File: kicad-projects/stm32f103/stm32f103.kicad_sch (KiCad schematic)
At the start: 68 parts, among them J1 Conn_01x20_Male, J2 USB_C_Receptacle, J3 Jack-DC, J4 Conn_02x02_Odd_Even, J5 Conn_01x10_Female, J6 Conn_01x06_Female, J7 Conn_01x08_Female, J8 Conn_01x08_Female, SW1 SW_Push, U1 TPS62175DQC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

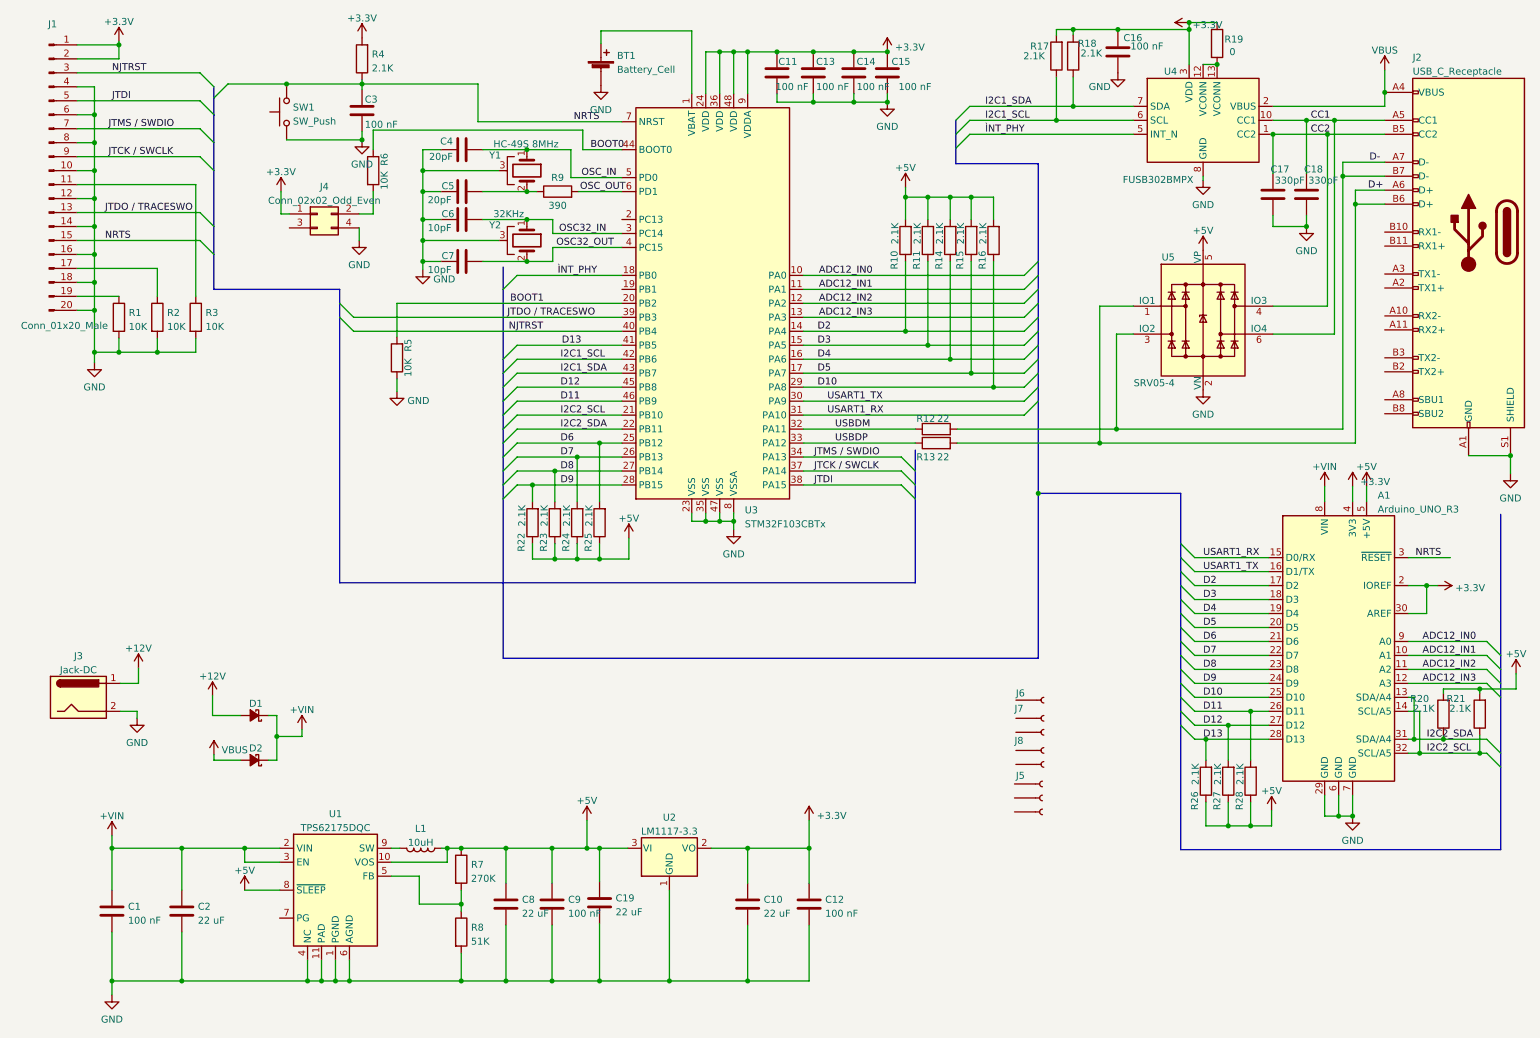
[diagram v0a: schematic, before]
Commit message: pcb: revision bump
stm32f103: revison 2
  - added: D+ to +5V (fixed error: unable to enumerate device)
  - added: usb phy int pin pull up to +3.3v (fixed no irq from phy)
  - moved: JTAG connector is moved to bottom layer

clock-top (nixie shild): revision 1, initial version

removed pf-info-cache (temp kicad file)
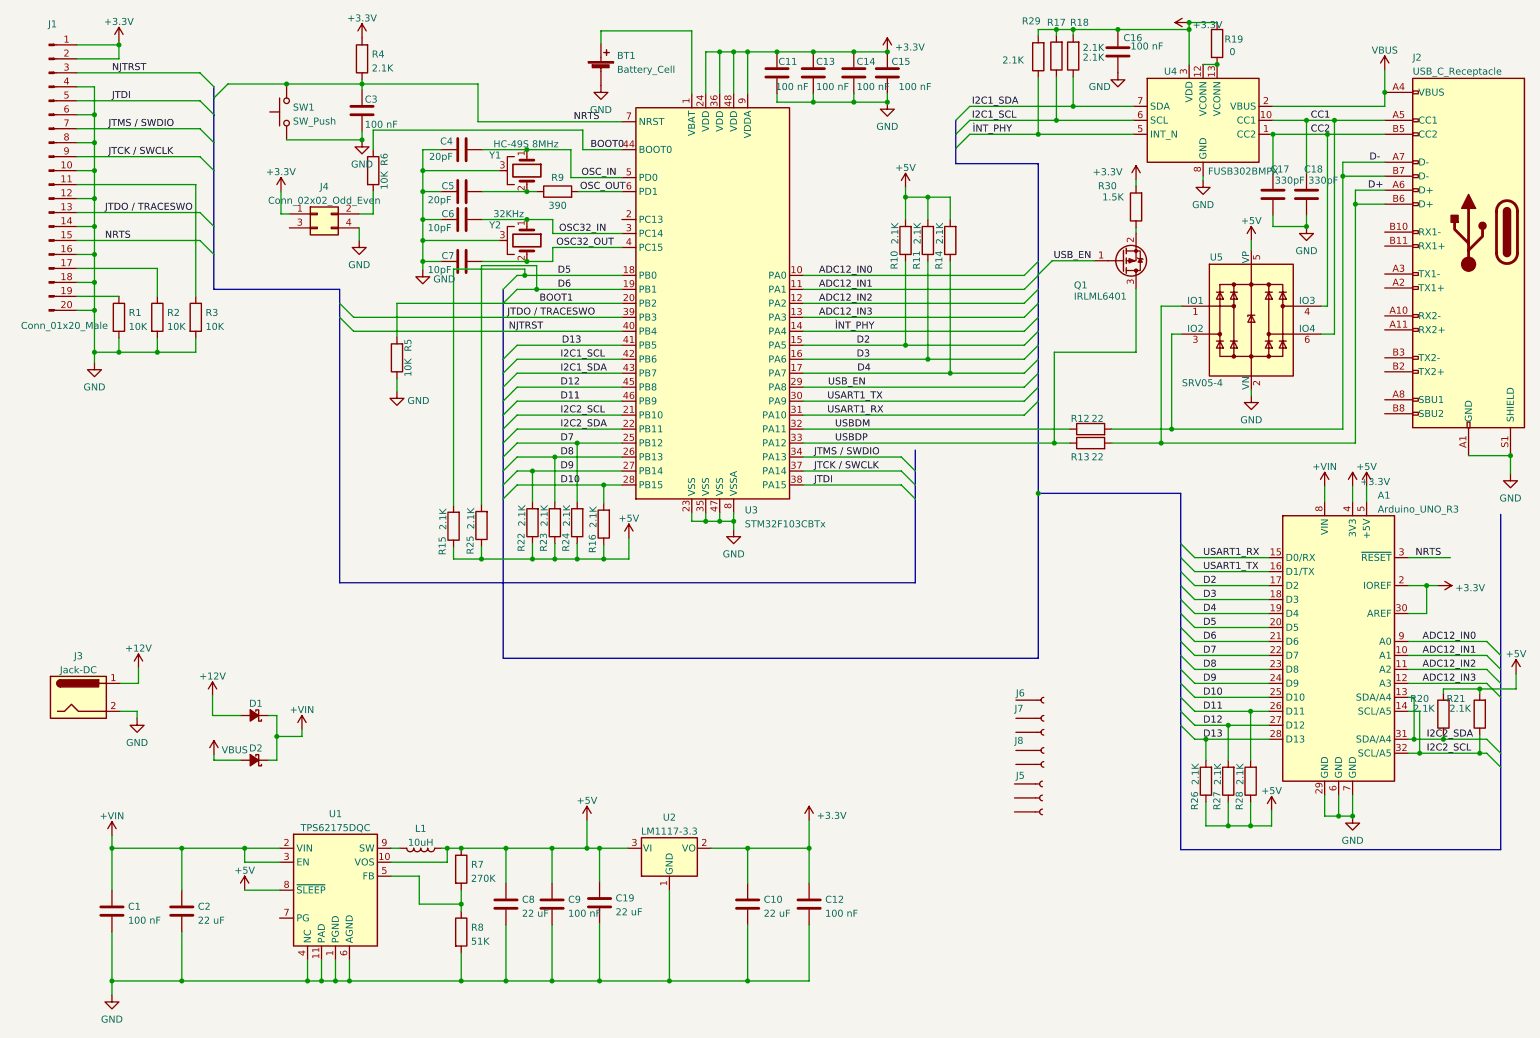
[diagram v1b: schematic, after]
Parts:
- added Q1: IRLML6401, Package_TO_SOT_SMD:SOT-23, symbol Transistor_FET:IRLML6401
- added R29: 2.1K, Resistor_SMD:R_0805_2012Metric_Pad1.20x1.40mm_HandSolder, symbol Device:R
- added R30: 1.5K, Resistor_SMD:R_0805_2012Metric_Pad1.20x1.40mm_HandSolder, symbol Device:R
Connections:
- net +3.3V: now also R29.2, R30.2
- net +5V: now also R15.1, R16.1; no longer R15.2, R16.2
- net D10: now also R16.2, U3.28 (PB15); no longer R16.1, U3.29 (PA8)
- net D2: now also U3.15 (PA5); no longer U3.14 (PA4)
- net D3: now also U3.16 (PA6); no longer U3.15 (PA5)
- net D4: now also U3.17 (PA7); no longer U3.16 (PA6)
- net D5: now also R15.2, U3.18 (PB0); no longer R15.1, U3.17 (PA7)
- net D6: now also U3.19 (PB1); no longer U3.25 (PB12)
- net D7: now also U3.25 (PB12); no longer U3.26 (PB13)
- net D8: now also U3.26 (PB13); no longer U3.27 (PB14)
- net D9: now also U3.27 (PB14); no longer U3.28 (PB15)
- net USBDP: now also Q1.3 (D)
- net ÌNT_PHY: now also U3.14 (PA4), R29.1; no longer U3.18 (PB0)
- new net: Q1.2 (S), R30.1
- new net USB_EN: Q1.1 (G), U3.29 (PA8)
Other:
- moved on the sheet: R12, R13, R15, R16, R25, U5
